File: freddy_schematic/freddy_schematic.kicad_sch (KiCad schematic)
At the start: 23 parts, among them K1 JZC-11F, K2 JZC-11F, Q1 P2N2222A, Q2 P2N2222A, SW1 Arcade Buttons, SW2 Arcade Button, SW3 Arcade Button, SW4 Arcade Button, SW5 Arcade Button, U1 ESP32-C3-DevKitC-02, U2 DFPlayer Mini, U3 ISD1820, U4 74HC595

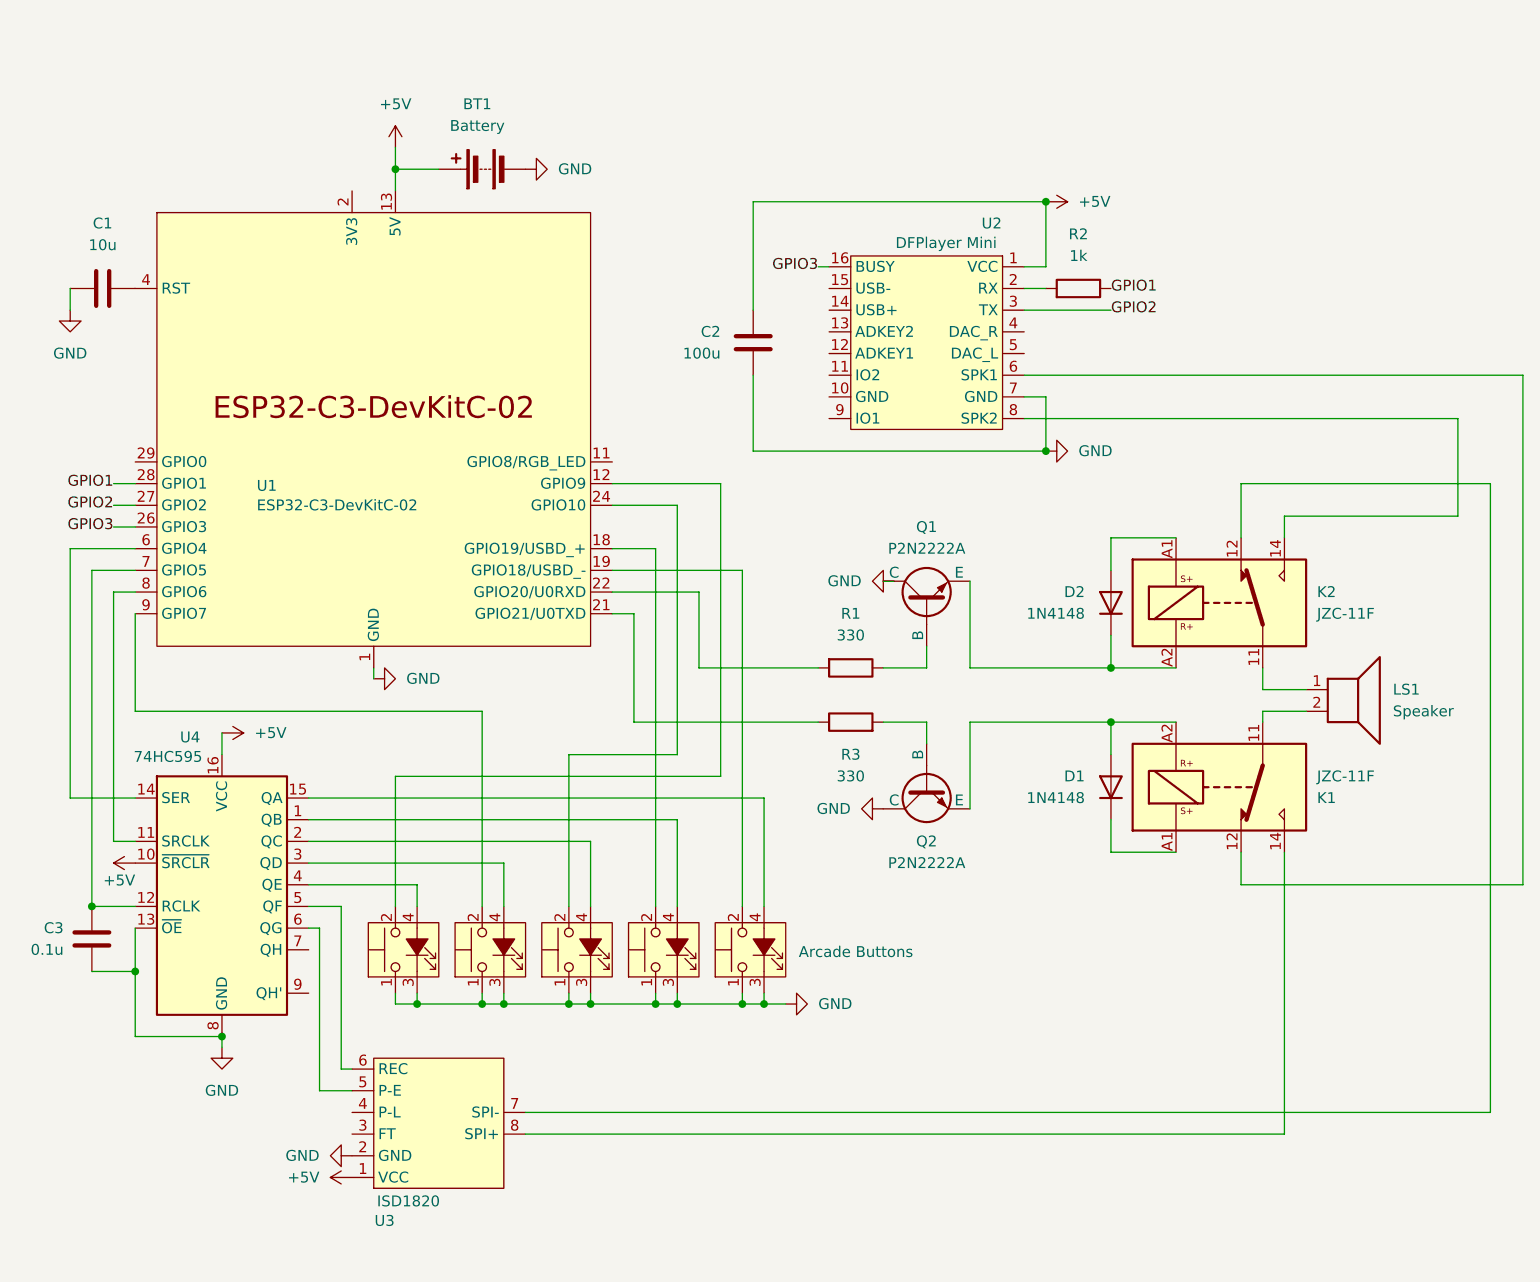
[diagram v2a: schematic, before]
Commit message: made playback a bit more consistent
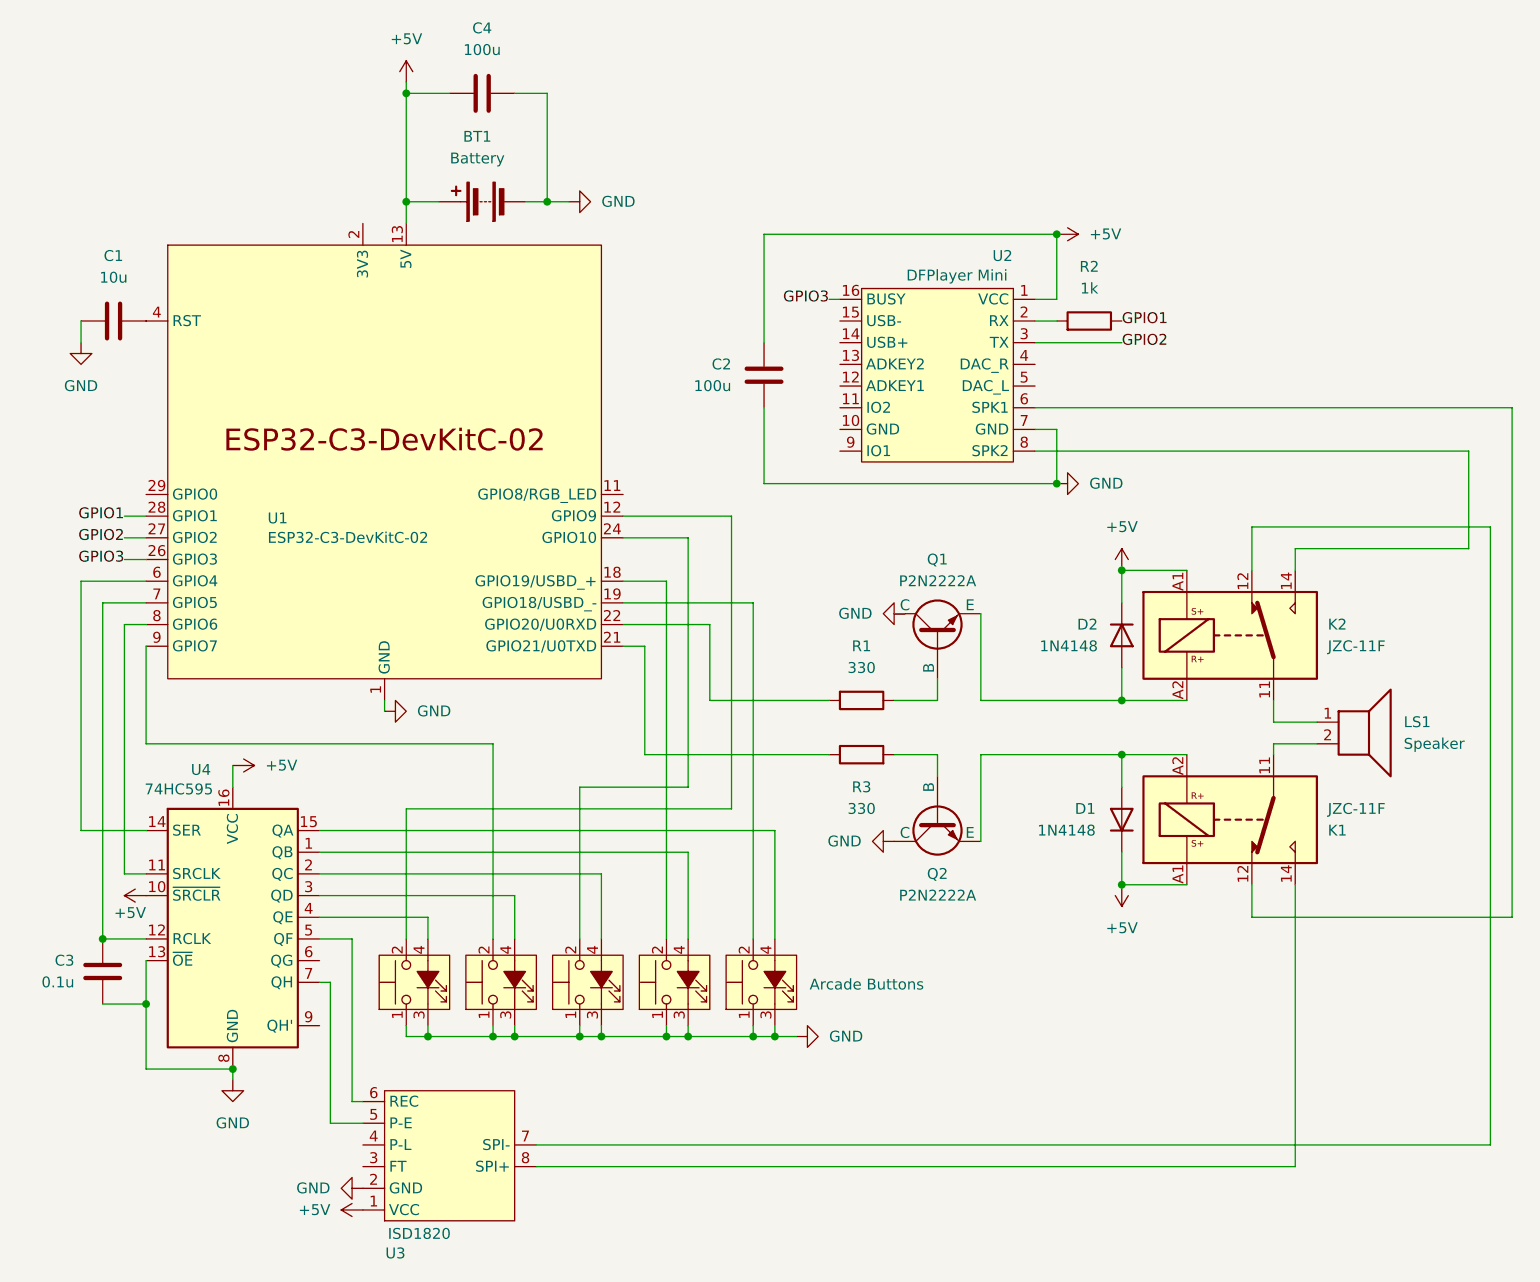
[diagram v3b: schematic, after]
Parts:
- added C4: 100u, symbol Device:C
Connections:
- net +5V: now also D1.1 (K), D2.1 (K), K1.A1, K2.A1, C4.2
- net GND: now also C4.1
- net at D2.2 (A): now also K2.A2, Q1.3 (E); no longer K2.A1
- net at U3.5 (P-E): now also U4.7 (QH); no longer U4.6 (QG)
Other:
- moved on the sheet: BT1, C1, C2, C3, D1, K1, K2, LS1, Q1, Q2, R1, R2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
